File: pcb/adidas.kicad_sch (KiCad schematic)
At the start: 31 parts, among them J1 ISP Header, J7 Battery, J9 Shitty Add-on, U1 MPU-6050, U2 ATTINY841-SSU

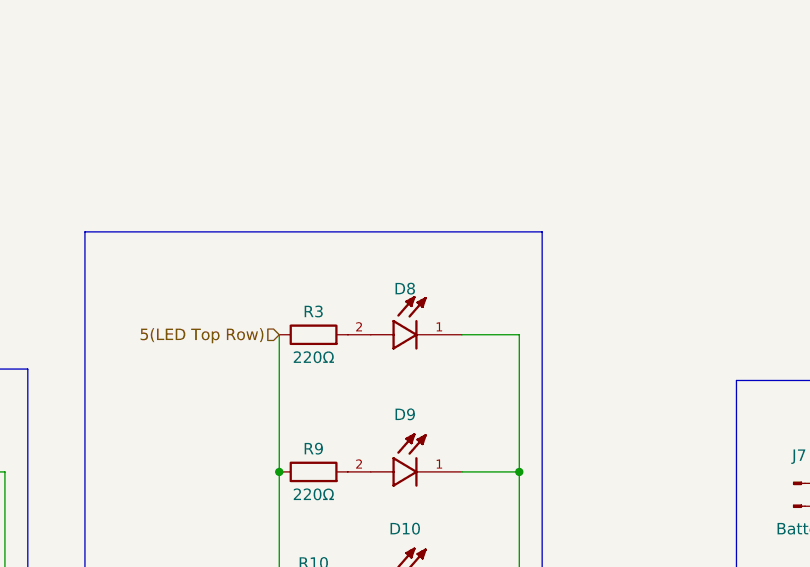
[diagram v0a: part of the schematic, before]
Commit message: make some changes from PCBway feedback v0.3
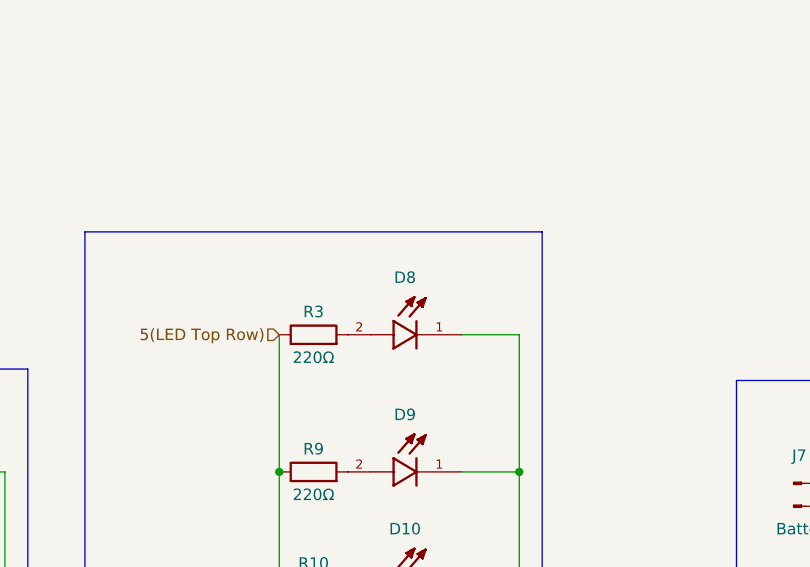
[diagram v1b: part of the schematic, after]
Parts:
- D1, D10, D12, D2, D3, D4, D5, D6, D7, D8, D9: value LHN974 -> AP3216SYCK; footprint LED_SMD:LED_0805_2012Metric -> LED_SMD:LED_1206_3216Metric; Color (none) -> Yellow; MANUFACTURER Valcon -> Kingbright; MAXIMUM_PACKAGE_HEIGHT 0.8mm -> 1.1mm
- D11: value ~ -> AP3216SYCK; footprint LED_SMD:LED_0805_2012Metric -> LED_SMD:LED_1206_3216Metric; Color (none) -> Yellow; MANUFACTURER Valcon -> Kingbright; MAXIMUM_PACKAGE_HEIGHT 0.8mm -> 1.1mm

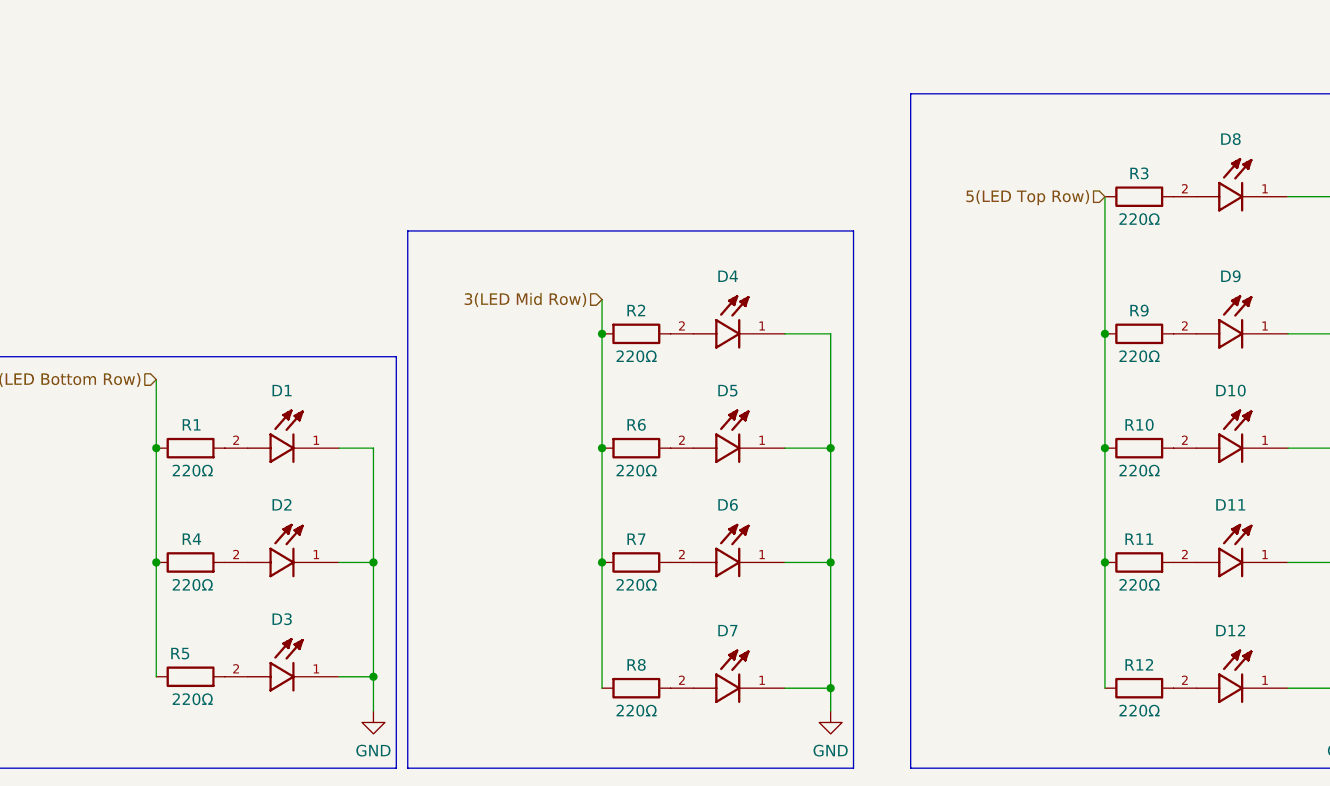
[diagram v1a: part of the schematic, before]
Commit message: add mouser and digikey part numbers
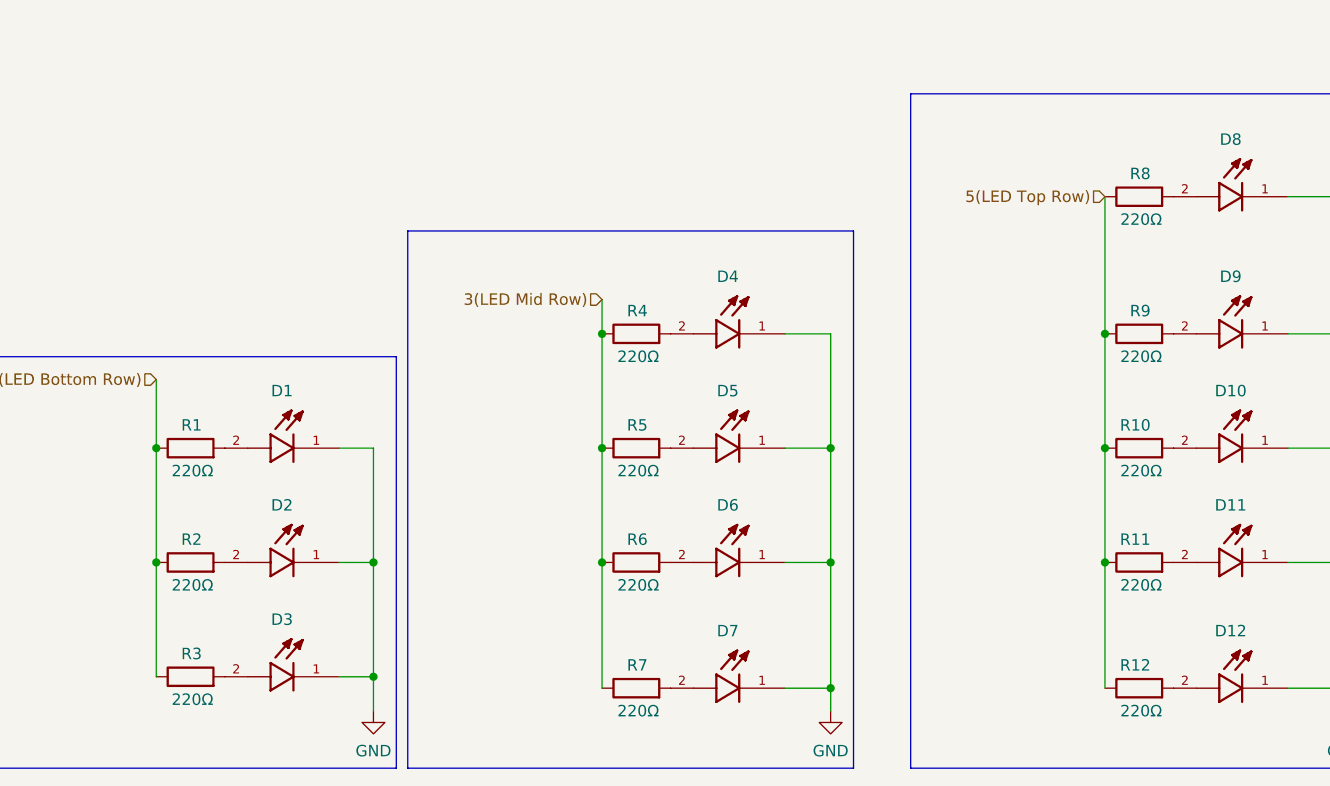
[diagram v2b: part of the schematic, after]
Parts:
- D1, D10, D11, D12, D2, D3, D4, D5, D6, D7, D8, D9: value AP3216SYCK -> CTL1206FWH1T; Color Yellow -> White; Digi-Key Part Number (none) -> 2679-CTL1206FWH1TTR-ND; MANUFACTURER Kingbright -> Venkel; MAXIMUM_PACKAGE_HEIGHT 1.1mm -> 1.2mm; PARTREV A -> (none)
- R1, R10, R11, R12, R2, R3, R4, R5, R6, R7, R8, R9: Digikey (none) -> https://www.digikey.com/en/products/detail/yageo/RC1206JR-0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; Manufacturer (none) -> YAGEO; Part (none) -> RC1206JR-07220RL
- S1: now left out of the parts list
- U1: AVAILABILITY Good -> (none); Mouser Part  (none) -> 410-MPU-6050; PARTREV 3.4 -> (none); PRICE 5.45 USD -> (none)
- U2: A1_MIN 0.1 -> (none); A_MAX 1.75 -> (none); A_MIN 1.75 -> (none); A_NOM 1.75 -> (none); B_MAX 0.5 -> (none); B_MIN 0.33 -> (none); B_NOM 0.415 -> (none); D2_MAX 0.0 -> (none); D_MAX 8.74 -> (none); D_MIN 8.55 -> (none); D_NOM 8.645 -> (none); E1_MAX 3.99 -> (none); E1_MIN 3.8 -> (none); E1_NOM 3.895 -> (none); E2_MAX 0.0 -> (none); ENOM 1.27 -> (none); E_MAX 6.19 -> (none); E_MIN 5.8 -> (none); E_NOM 5.995 -> (none); L_MAX 1.27 -> (none); L_MIN 0.41 -> (none); L_NOM 0.84 -> (none); Mouser Part (none) -> 556-ATTINY841-SSU; PACKAGE_TYPE (none) -> SOIC-14; PARTREV A -> (none); PIN_COUNT 14.0 -> (none); STANDARD IPC 7351B -> (none)
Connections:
- net 2(LED Bottom Row): now also R2.1, R3.1; no longer R4.1, R5.1
- net 3(LED Mid Row): now also R4.1, R5.1, R6.1, R7.1; no longer R2.2, R6.2, R7.2, R8.2
- net 5(LED Top Row): now also R8.1; no longer R3.1
- net at D5.2: now also R5.2; no longer R6.1
- net at D6.2: now also R6.2; no longer R7.1
- net at D4.2: now also R4.2; no longer R2.1
- net at D3.2: now also R3.2; no longer R5.2
- net at D2.2: now also R2.2; no longer R4.2
- net at D8.2: now also R8.2; no longer R3.2
- net at D7.2: now also R7.2; no longer R8.1

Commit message: run ERC checks
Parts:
- R1: Manufacturer Product Number (none) -> RC1206JR-07220RL; Part RC1206JR-07220RL -> (none)
- R13: Digi-Key Part Number (none) -> 311-10KERCT-ND; Manufacturer (none) -> YAGEO; Manufacturer Product Number (none) -> RC1206JR-0710KL
- S1: Digi-Key Part Number (none) -> SW400-ND; MANUFACTURER Omron -> (none); Manufacturer (none) -> Omron Electronics Inc-EMC Div
- U1: footprint DEAD10C5:QFN50P400X400X95-24N -> QFN50P400X400X95-24N; symbol MPU-6050:MPU-6050 -> dead10c5:MPU-6050; AVAILABILITY (none) -> Good; Manufacturer (none) -> TDK; Manufacturer Product Number (none) -> MPU-6050; PARTREV (none) -> 3.4; PRICE (none) -> 5.45 USD
- U2: footprint DEAD10C5:SOIC127P599X175-14N -> SOIC127P599X175-14N; symbol ATTINY841-SSU:ATTINY841-SSU -> dead10c5:ATTINY841-SSU; A1_MIN (none) -> 0.1; A_MAX (none) -> 1.75; A_MIN (none) -> 1.75; A_NOM (none) -> 1.75; B_MAX (none) -> 0.5; B_MIN (none) -> 0.33; B_NOM (none) -> 0.415; D2_MAX (none) -> 0.0; D_MAX (none) -> 8.74; D_MIN (none) -> 8.55; D_NOM (none) -> 8.645; E1_MAX (none) -> 3.99; E1_MIN (none) -> 3.8; E1_NOM (none) -> 3.895; E2_MAX (none) -> 0.0; ENOM (none) -> 1.27; E_MAX (none) -> 6.19; E_MIN (none) -> 5.8; E_NOM (none) -> 5.995; L_MAX (none) -> 1.27; L_MIN (none) -> 0.41; L_NOM (none) -> 0.84; Manufacturer (none) -> Microchip; PARTREV (none) -> A; PIN_COUNT (none) -> 14.0; STANDARD (none) -> IPC 7351B
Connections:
- net VCC +3.3V is gone; now on net VDD: J9.1 (Pin_1)
- net +BATT renamed VDD
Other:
- moved on the sheet: J7

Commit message: run ERC checks (#28)
* run ERC checks

* kibot testing
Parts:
- U1: footprint QFN50P400X400X95-24N -> DEAD10C5:QFN50P400X400X95-24N
- U2: footprint SOIC127P599X175-14N -> DEAD10C5:SOIC127P599X175-14N
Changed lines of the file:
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@@
       (effects (font (size 1.27 1.27)))
     )
-    (property "Footprint" "SOIC127P599X175-14N" (at 146.05 66.04 0)
+    (property "Footprint" "DEAD10C5:SOIC127P599X175-14N" (at 146.05 66.04 0)
       (effects (font (size 1.27 1.27)) (justify left bottom) hide)
     )
@@
       (effects (font (size 1.27 1.27)))
     )
-    (property "Footprint" "QFN50P400X400X95-24N" (at 80.01 66.04 0)
-      (effects (font (size 1.27 1.27)) (justify left bottom) hide)
-    )
+    (property "Footprint" "DEAD10C5:QFN50P400X400X95-24N" (at 80.01 66.04 0)
+      (effects (font (size 1.27 1.27)) (justify left bottom) hide)
+    )

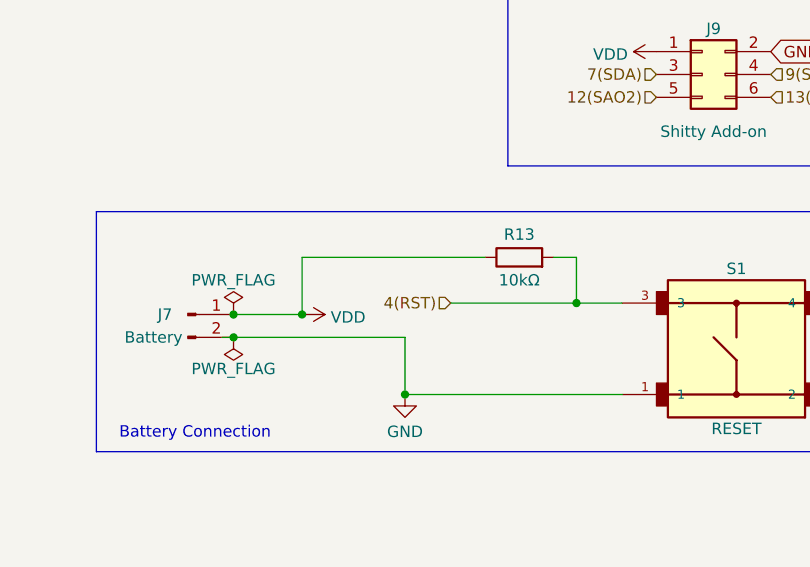
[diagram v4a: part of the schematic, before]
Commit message: BOM updates (#29)
* update schematic

* update schematic

* update the battery clip in the BOM
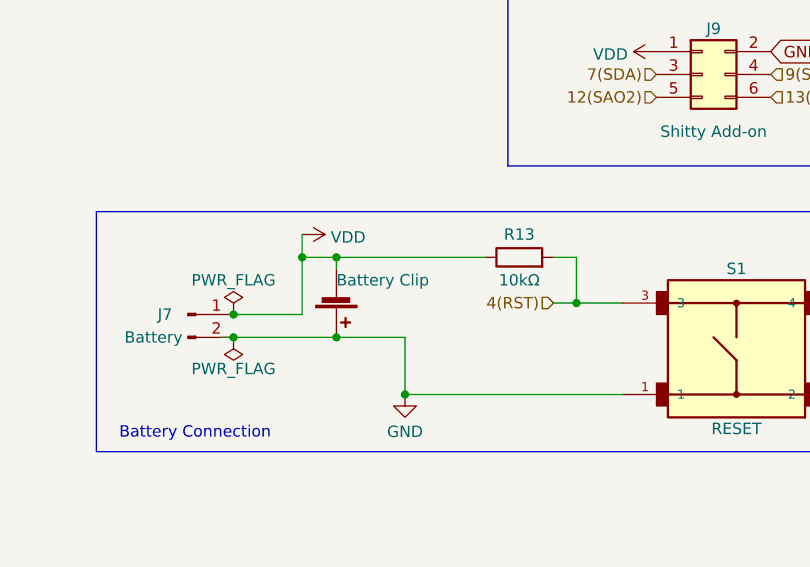
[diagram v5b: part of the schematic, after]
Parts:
- added BT1: Battery Clip, DEAD10C5:BatteryHolder_Keystone_3002_1x2032, symbol Device:Battery_Cell
- D10: MANUFACTURER Venkel -> (none); Manufacturer (none) -> Venkel
- U1: AVAILABILITY Good -> (none); MF TDK -> (none); PARTREV 3.4 -> (none); PRICE 5.45 USD -> (none); STANDARD IPC-7351B -> (none)
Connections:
- net GND: now also BT1.1 (+)
- net VDD: now also BT1.2 (-)
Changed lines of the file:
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@@
-(kicad_sch (version 20230121) (generator eeschema)
+(kicad_sch (version 20230221) (generator eeschema)
   (paper "A4")
   (title_block
@@
     (comment 1 "Русский хардбасс")
   )
+  (junction (at 219.71 151.13) (diameter 0) (color 0 0 0 0)
+  )
   (junction (at 208.28 151.13) (diameter 0) (color 0 0 0 0)
   )
@@
   (junction (at 36.83 160.02) (diameter 0) (color 0 0 0 0)
   )
+  (junction (at 215.9 142.24) (diameter 0) (color 0 0 0 0)
+  )
   (junction (at 168.91 186.69) (diameter 0) (color 0 0 0 0)
   )
-  (junction (at 215.9 148.59) (diameter 0) (color 0 0 0 0)
-  )
   (junction (at 111.76 186.69) (diameter 0) (color 0 0 0 0)
   )
@@
   )
   (junction (at 36.83 172.72) (diameter 0) (color 0 0 0 0)
+  )
+  (junction (at 219.71 142.24) (diameter 0) (color 0 0 0 0)
   )
   (junction (at 86.36 160.02) (diameter 0) (color 0 0 0 0)
@@
     (stroke (width 0) (type default))
   )
+  (wire (pts (xy 219.71 151.13) (xy 227.33 151.13))
+    (stroke (width 0) (type default))
+  )
   (wire (pts (xy 113.03 71.12) (xy 113.03 45.72))
     (stroke (width 0) (type default))
@@
     (stroke (width 0) (type default))
   )
+  (wire (pts (xy 219.71 142.24) (xy 236.22 142.24))
+    (stroke (width 0) (type default))
+  )
+  (wire (pts (xy 219.71 142.24) (xy 219.71 143.51))
+    (stroke (width 0) (type default))
+  )
+  (wire (pts (xy 215.9 139.7) (xy 215.9 142.24))
+    (stroke (width 0) (type default))
+  )
   (wire (pts (xy 111.76 172.72) (xy 111.76 186.69))
     (stroke (width 0) (type default))
@@
     (stroke (width 0) (type default))
   )
-  (wire (pts (xy 215.9 142.24) (xy 236.22 142.24))
+  (wire (pts (xy 215.9 142.24) (xy 219.71 142.24))
     (stroke (width 0) (type default))
   )
@@
     (stroke (width 0) (type default))
   )
-  (wire (pts (xy 208.28 151.13) (xy 227.33 151.13))
+  (wire (pts (xy 208.28 151.13) (xy 219.71 151.13))
     (stroke (width 0) (type default))
   )
@@
     (stroke (width 0) (type default))
   )
-  (wire (pts (xy 232.41 147.32) (xy 246.38 147.32))
+  (wire (pts (xy 243.84 147.32) (xy 246.38 147.32))
     (stroke (width 0) (type default))
   )
@@
     (effects (font (size 1.27 1.27)) (justify right))
   )
-  (hierarchical_label "4(RST)" (shape input) (at 232.41 147.32 180) (fields_autoplaced)
+  (hierarchical_label "4(RST)" (shape input) (at 243.84 147.32 180) (fields_autoplaced)
     (effects (font (size 1.27 1.27)) (justify right))
   )
@@
       (effects (font (size 1.27 1.27)) (justify bottom) hide)
     )
-    (property "MANUFACTURER" "Venkel" (at 157.48 160.02 0)
+    (property "Manufacturer" "Venkel" (at 157.48 160.02 0)
       (effects (font (size 1.27 1.27)) (justify bottom) hide)
     )
@@
     )
   )
-  (symbol (lib_id "power:VDD") (at 215.9 148.59 270) (mirror x) (unit 1)
-    (in_bom yes) (on_board yes) (dnp no)
-    (property "Reference" "#PWR01" (at 212.09 148.59 0)
-      (effects (font (size 1.27 1.27)) hide)
-    )
-    (property "Value" "VDD" (at 219.075 148.9068 90)
-      (effects (font (size 1.27 1.27)) (justify left))
-    )
-    (property "Footprint" "" (at 215.9 148.59 0)
-      (effects (font (size 1.27 1.27)) hide)
-    )
-    (property "Datasheet" "" (at 215.9 148.59 0)
+  (symbol (lib_id "power:VDD") (at 215.9 139.7 270) (mirror x) (unit 1)
+    (in_bom yes) (on_board yes) (dnp no)
+    (property "Reference" "#PWR01" (at 212.09 139.7 0)
+      (effects (font (size 1.27 1.27)) hide)
+    )
+    (property "Value" "VDD" (at 219.075 140.0168 90)
+      (effects (font (size 1.27 1.27)) (justify left))
+    )
+    (property "Footprint" "" (at 215.9 139.7 0)
+      (effects (font (size 1.27 1.27)) hide)
+    )
+    (property "Datasheet" "" (at 215.9 139.7 0)
       (effects (font (size 1.27 1.27)) hide)
     )
@@
     )
   )
+  (symbol (lib_id "Device:Battery_Cell") (at 219.71 146.05 0) (mirror x) (unit 1)
+    (in_bom no) (on_board yes) (dnp no)
+    (property "Reference" "BT1" (at 222.631 148.7257 0)
+      (effects (font (size 1.27 1.27)) (justify left) hide)
+    )
+    (property "Value" "Battery Clip" (at 219.71 144.78 0)
+      (effects (font (size 1.27 1.27)) (justify left))
+    )
+    (property "Footprint" "DEAD10C5:BatteryHolder_Keystone_3002_1x2032" (at 219.71 147.574 90)
+      (effects (font (size 1.27 1.27)) hide)
+    )
+    (property "Datasheet" "https://www.mouser.com/datasheet/2/215/3000TR-742873.pdf" (at 219.71 147.574 90)
+      (effects (font (size 1.27 1.27)) hide)
+    )
+    (property "Mouser Part Number`" "534-3000TR" (at 219.71 146.05 0)
+      (effects (font (size 1.27 1.27)) hide)
+    )
+    (property "Manufacturer Product Number" "3000TR" (at 219.71 146.05 0)
+      (effects (font (size 1.27 1.27)) hide)
+    )
+    (property "Manufacturer" "Keystone Electronics" (at 219.71 146.05 0)
+      (effects (font (size 1.27 1.27)) hide)
+    )
+    (property "Description" "CR2032 Coin Cell Battery Holder" (at 219.71 146.05 0)
+      (effects (font (size 1.27 1.27)) hide)
+    )
+    (pin "1")
+    (pin "2")
+    (instances
+      (project "adidas"
+        (path "/8f89af5e-dffe-4a05-a949-99c4cebef567"
+          (reference "BT1") (unit 1)
+        )
+      )
+    )
+  )
   (symbol (lib_id "Device:R") (at 146.05 147.32 90) (unit 1)
     (in_bom yes) (on_board yes) (dnp no)
@@
       (effects (font (size 1.27 1.27)) (justify left bottom) hide)
     )
-    (property "STANDARD" "IPC-7351B" (at 80.01 66.04 0)
-      (effects (font (size 1.27 1.27)) (justify left bottom) hide)
-    )
-    (property "PRICE" "5.45 USD" (at 80.01 66.04 0)
-      (effects (font (size 1.27 1.27)) (justify left bottom) hide)
-    )
     (property "DESCRIPTION" "IMU ACCEL/GYRO 3-AXIS I2C 24QFN" (at 80.01 66.04 0)
       (effects (font (size 1.27 1.27)) (justify left bottom) hide)
     )
-    (property "MF" "TDK" (at 80.01 66.04 0)
-      (effects (font (size 1.27 1.27)) (justify left bottom) hide)
-    )
-    (property "PARTREV" "3.4" (at 80.01 66.04 0)
-      (effects (font (size 1.27 1.27)) (justify left bottom) hide)
-    )
-    (property "AVAILABILITY" "Good" (at 80.01 66.04 0)
-      (effects (font (size 1.27 1.27)) (justify left bottom) hide)
-    )
